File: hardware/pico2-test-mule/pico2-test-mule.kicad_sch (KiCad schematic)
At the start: 71 parts, among them J2 SPEAKER, J4 POWER, J5 EXT_CAP, J6 RAILS, J7 AUX, J8 MOTOR, Q1 DMN2991UDA-7B, Q10 SS8050, Q11 SS8050, Q12 SS8050, Q13 SS8050, Q2 DMN2991UDA-7B, Q3 NST847BPDP6T5G, Q4 NST847BPDP6T5G, Q5 DMN2991UDA-7B, Q6 DMN2991UDA-7B, Q7 DMN2991UDA-7B, Q8 DMN2991UDA-7B, Q9 SS8050, U1 NCS2220AMUT1G, U2 AP63203WU, U5 MAX98357AEWL+T, U6 MD9927, U7 PICO

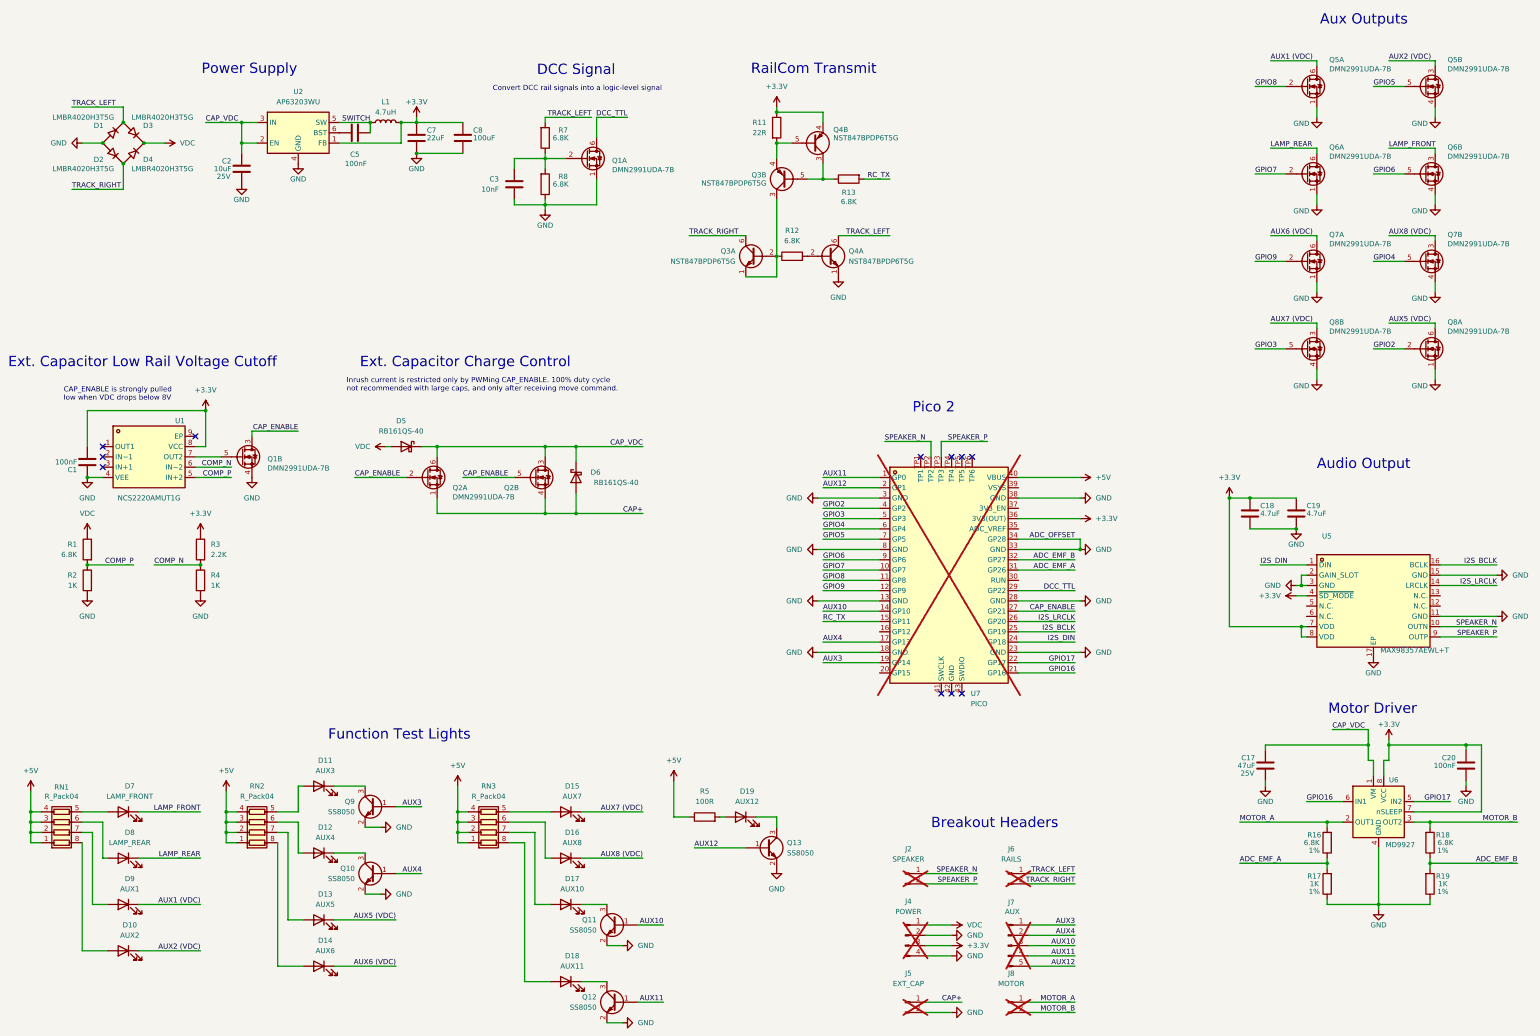
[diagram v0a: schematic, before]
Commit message: fix: combine left side headers
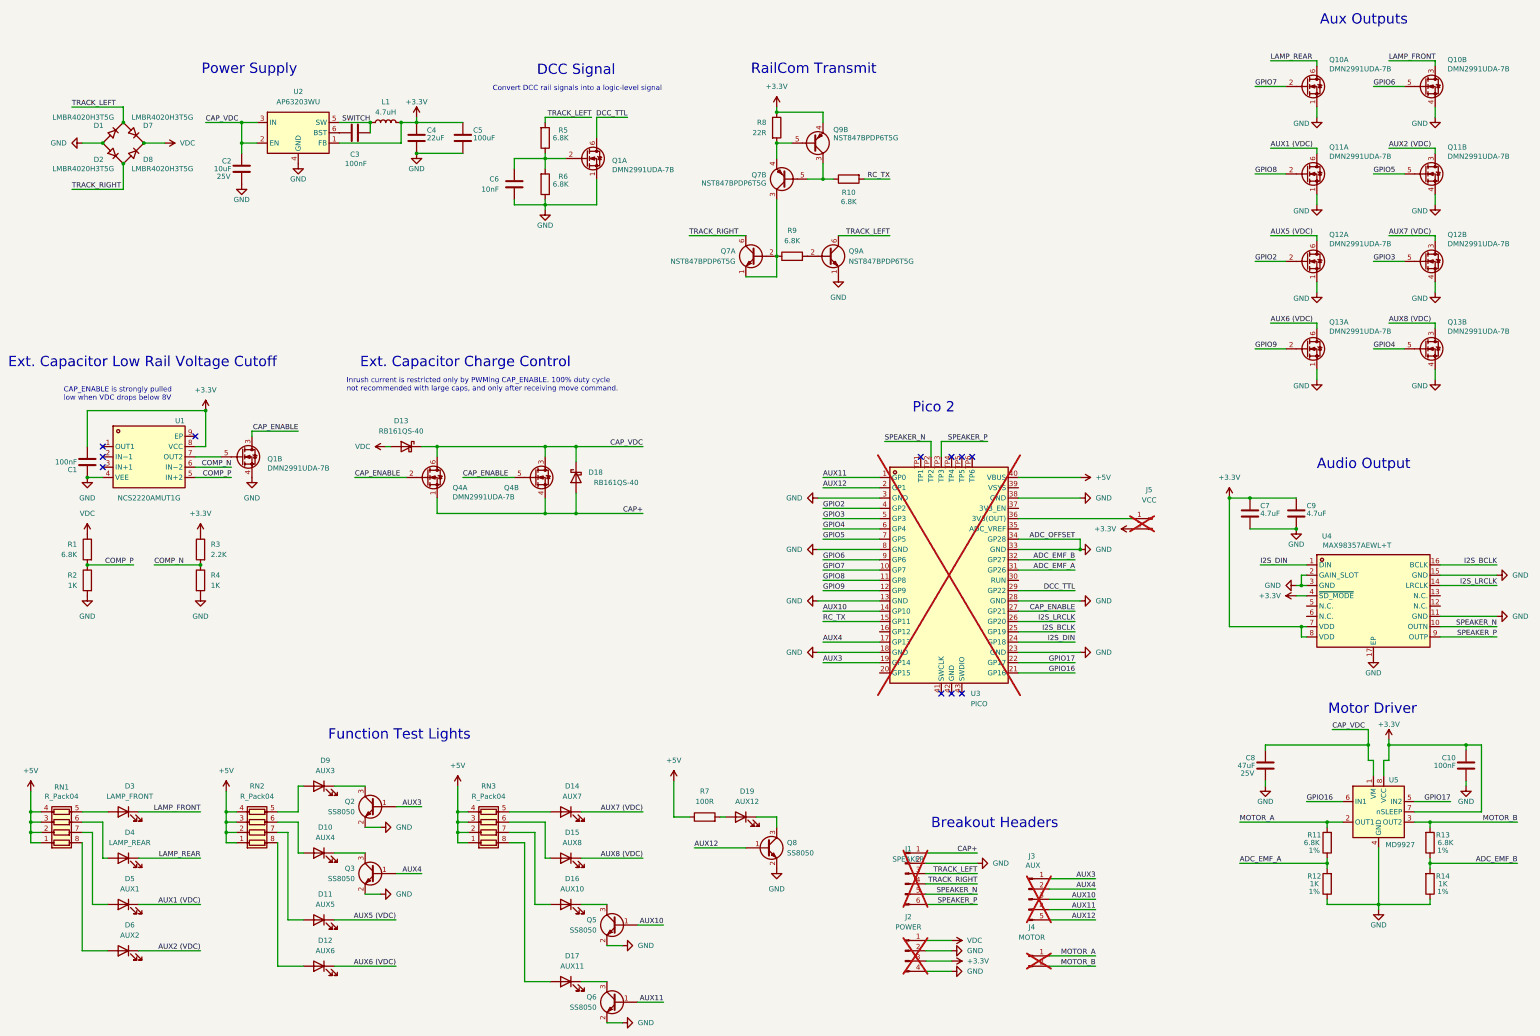
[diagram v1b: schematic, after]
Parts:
- removed J6: RAILS, Connector_PinHeader_2.54mm:PinHeader_1x02_P2.54mm_Vertical, symbol pico2-test-mule:Conn_01x02_Pin
- J1: renamed from J2; footprint Connector_PinHeader_2.54mm:PinHeader_1x02_P2.54mm_Vertical -> Connector_PinHeader_2.54mm:PinHeader_1x06_P2.54mm_Vertical; symbol pico2-test-mule:Conn_01x02_Pin -> pico2-test-mule:Conn_01x06_Pin; now in the parts list
- J5: value EXT_CAP -> VCC
- renumbered C20 to C10, C5 to C3, C7 to C4, C8 to C5, C3 to C6, C18 to C7, C17 to C8, C19 to C9, D12 to D10, D13 to D11, D14 to D12, D5 to D13, D15 to D14, D16 to D15, D17 to D16, D18 to D17, D6 to D18, D7 to D3, D8 to D4, D9 to D5, D10 to D6, D3 to D7, D4 to D8, D11 to D9, J4 to J2, J7 to J3, J8 to J4, Q6 to Q10, Q5 to Q11, Q8 to Q12, Q7 to Q13, Q9 to Q2, Q10 to Q3, Q2 to Q4, Q11 to Q5, Q12 to Q6, Q3 to Q7, Q13 to Q8, Q4 to Q9, R13 to R10, R16 to R11, R17 to R12, R18 to R13, R19 to R14, R7 to R5, R8 to R6, R5 to R7, R11 to R8, R12 to R9, U7 to U3, U5 to U4, U6 to U5
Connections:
- net +3.3V: now also J5.2 (Pin_2); no longer U3.36 (3V3(OUT))
- net CAP+: now also J1.1 (Pin_1); no longer J5.1 (Pin_1)
- net GND: now also J1.2 (Pin_2); no longer J5.2 (Pin_2)
- net SPEAKER_N: now also J1.5 (Pin_5); no longer J1.1 (Pin_1)
- net SPEAKER_P: now also J1.6 (Pin_6); no longer J1.2 (Pin_2)
- net TRACK_LEFT: now also J1.3 (Pin_3)
- net TRACK_RIGHT: now also J1.4 (Pin_4)
- new net: J5.1 (Pin_1), U3.36 (3V3(OUT))
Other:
- moved on the sheet: J2, J3, J4, Q10A, Q10B, Q11A, Q11B, Q12A, Q12B, Q13A, Q13B

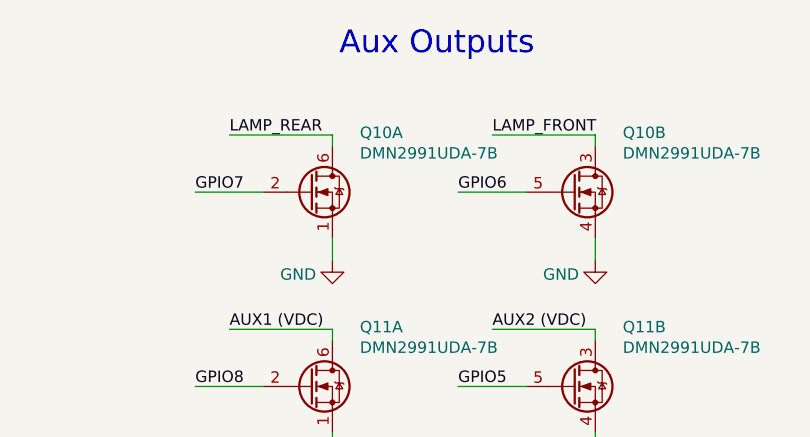
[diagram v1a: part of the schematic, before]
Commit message: chore: rearrange labels
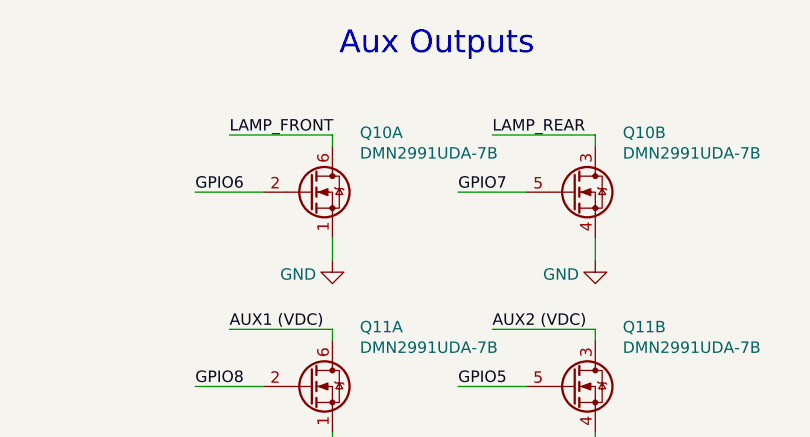
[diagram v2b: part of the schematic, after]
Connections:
- net GPIO6: now also Q10.2 (G1); no longer Q10.5 (G2)
- net GPIO7: now also Q10.5 (G2); no longer Q10.2 (G1)
- net LAMP_FRONT: now also Q10.6 (D1); no longer Q10.3 (D2)
- net LAMP_REAR: now also Q10.3 (D2); no longer Q10.6 (D1)
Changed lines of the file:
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@@
 	)
 	(label "LAMP_REAR"
-		(at 334.01 33.02 0)
+		(at 363.22 33.02 0)
 		(effects
 			(font
@@
 	)
 	(label "LAMP_FRONT"
-		(at 363.22 33.02 0)
+		(at 334.01 33.02 0)
 		(effects
 			(font
@@
 	)
 	(label "GPIO6"
-		(at 359.41 39.37 0)
+		(at 330.2 39.37 0)
 		(effects
 			(font
@@
 	)
 	(label "GPIO7"
-		(at 330.2 39.37 0)
-		(effects
-			(font
+		(at 359.41 39.37 0)
+		(effects
+			(font
